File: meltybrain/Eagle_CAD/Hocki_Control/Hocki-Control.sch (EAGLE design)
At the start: 123 parts, among them J1 SM03B-SRSS-TB(LF)(SN), J2 SM03B-SRSS-TB(LF)(SN), J3 SM03B-SRSS-TB(LF)(SN), J4 SM04B-SRSS-TB(LF)(SN), J5 SM04B-SRSS-TB(LF)(SN), U1 TEENSY_4.1, U10 TLV3502AIDCNR, U11 NL27WZ32USG, U12 NL27WZ32USG, U13 HMC1052L-TR, U14 LMV358, U15 IRF7509, U16 TMUX1219DCKR, U17 LMV358, U18 LMV358, U19 AP2210K-3.3TRG1, U2 ADXL375, U20 AP2210K-5.0TRG1, U21 AP63200, U22 74AHC1G04GW,125, U23 LDL212PU50R, U3 ADXL375, U4 ADXL375, U5 ADXL375, U6 LMH6612MAX/NOPB, U7 LMH6612MAX/NOPB, U8 LMH6612MAX/NOPB, U9 LMH6612MAX/NOPB

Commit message: accs moved
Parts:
- added D3: D26V0H1U2LP20-7, Hocki_Library:D26V0H1U2LP20-7
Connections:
- net +24V: now also D3.C
- net CS3: now also U1.10/PWM/MQSR/CS; no longer U1.9/PWM/OUT1C
- net CS4: now also U1.24/PWM/SCL2/TX6/A10; no longer U1.10/PWM/MQSR/CS
- net GND: now also D3.A
- net INT1A: now also U1.41/A17; no longer U1.40/A16
- net INT1B: now also U1.40/A16; no longer U1.41/A17
- net INT3A: now also U1.7/PWM/OUT1A/RX2; no longer U1.8/PWM/IN1/TX2
- net INT3B: now also U1.8/PWM/IN1/TX2; no longer U1.7/PWM/OUT1A/RX2
- net INT4B: now also U1.26/MOSI1/A12; no longer U1.24/PWM/SCL2/TX6/A10

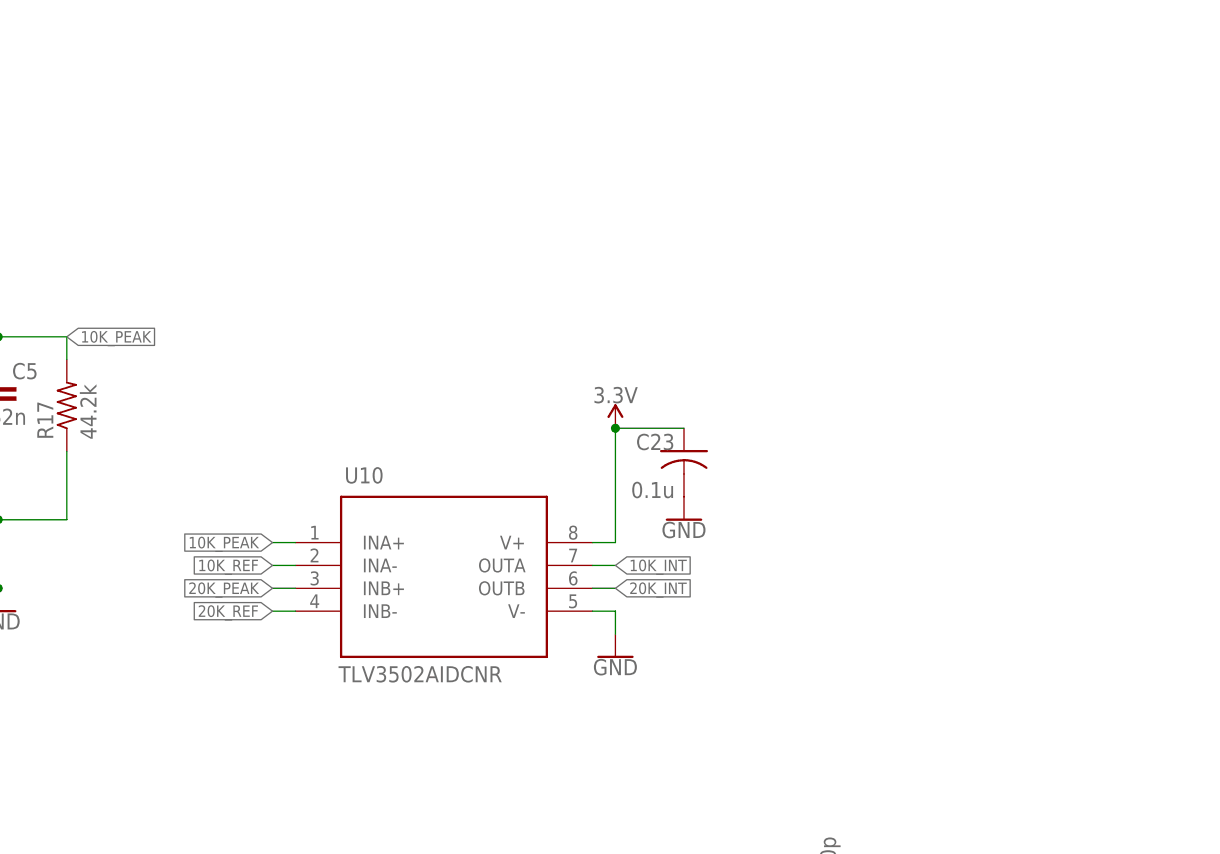
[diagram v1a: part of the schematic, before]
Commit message: added comparator hysteresis
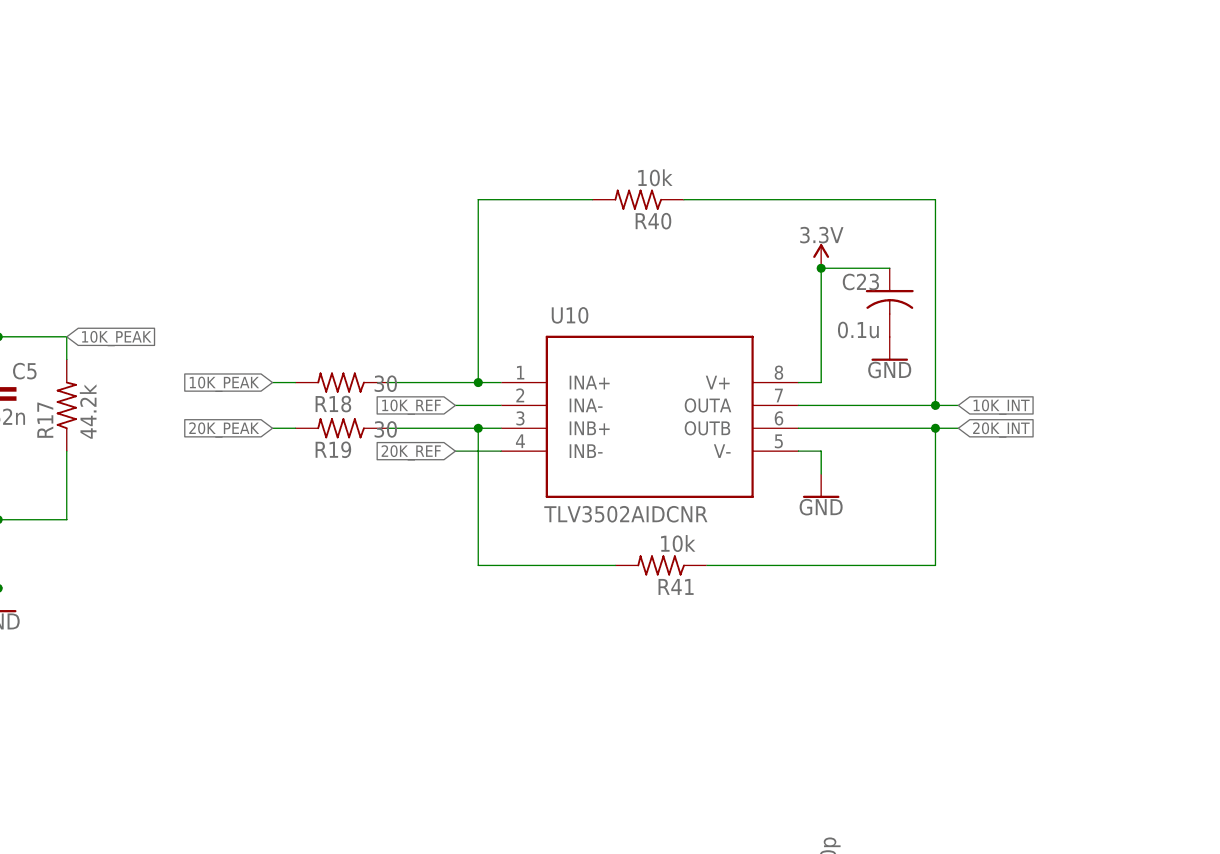
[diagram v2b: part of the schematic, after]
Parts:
- added R18, R19: 30, rcl:R-US_R0603
- added R40, R41: 10k, rcl:R-US_R0603
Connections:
- new net N$5: R18.1, R40.2, U10.INA+
- new net N$6: R19.1, R41.2, U10.INB+
- net 10K_INT: now also R40.1
- net 10K_PEAK: now also R18.2; no longer U10.INA+
- net 20K_INT: now also R41.1
- net 20K_PEAK: now also R19.2; no longer U10.INB+
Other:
- moved on the sheet: C23, U10

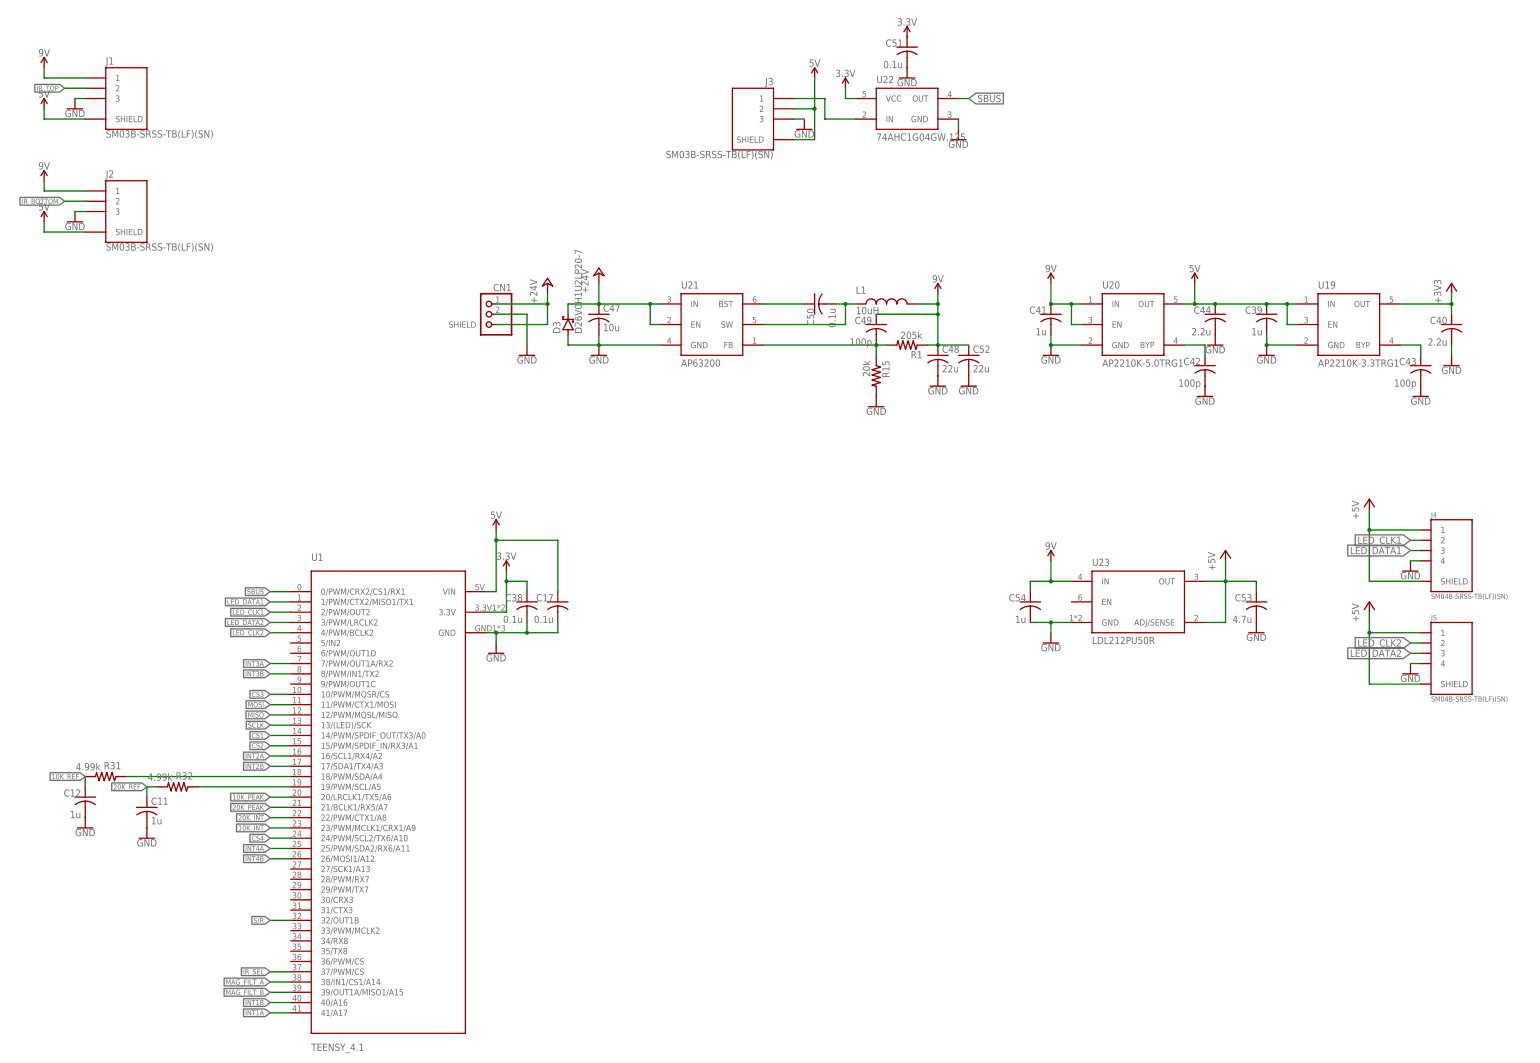
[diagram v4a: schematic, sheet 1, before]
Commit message: control schematic done
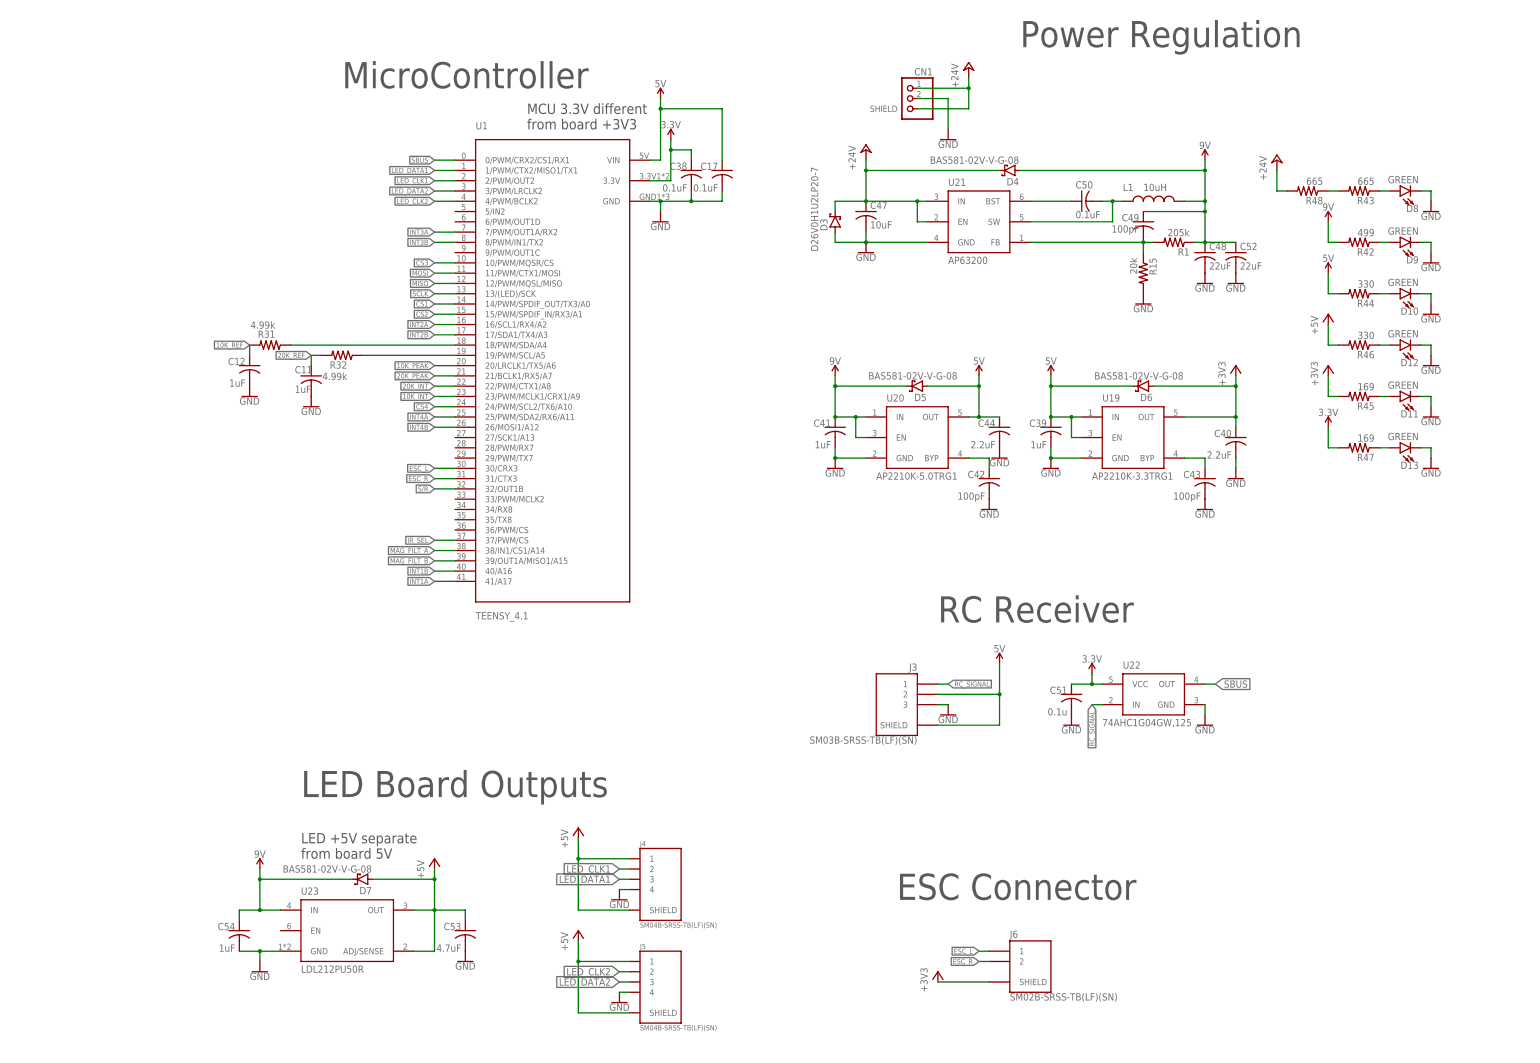
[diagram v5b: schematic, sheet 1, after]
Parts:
- added D10, D11, D12, D13, D8, D9: GREEN, SparkFun-LED:LED-GREEN0603
- added D4, D5, D6, D7: BAS581-02V-V-G-08, Hocki_Library:BAS581-02V-V-G-08
- added J6: SM02B-SRSS-TB(LF)(SN), Hocki_Library:SM02B-SRSS-TB(LF)(SN)
- added R42: 499, rcl:R-US_R0603
- added R43, R48: 665, rcl:R-US_R0603
- added R44, R46: 330, rcl:R-US_R0603
- added R45, R47: 169, rcl:R-US_R0603
- C1, C13, C15, C2, C3, C4, C45, C46: value 47n -> 47nF
- C11, C12, C39, C41, C54: value 1u -> 1uF
- C14, C16: value 0.18u -> 0.18uF
- C17, C18, C19, C20, C21, C22, C23, C24, C25, C26, C27, C28, C29, C30, C31, C32, C33, C34, C35, C36, C37, C38, C50: value 0.1u -> 0.1uF
- C40, C44: value 2.2u -> 2.2uF
- C42, C43, C49: value 100p -> 100pF
- C47: value 10u -> 10uF
- C48, C52: value 22u -> 22uF
- C5, C6: value 62n -> 62nF
- C53: value 4.7u -> 4.7uF
- C7, C9: value 1000p -> 1000pF
- C8: value .1u -> .1uF
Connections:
- net N$17 renamed RC_SIGNAL
- new net ESC_L: J6.1, U1.30/CRX3
- new net ESC_R: J6.2, U1.31/CTX3
- new net N$14: D12.A, R46.1
- new net N$15: D10.A, R44.1
- new net N$17: D11.A, R45.1
- new net N$18: D9.A, R42.1
- new net N$19: D8.A, R43.1
- new net N$20: R43.2, R48.1
- new net N$27: D13.A, R47.1
- net +24V: now also D4.C, R48.2
- net +3V3: now also D6.A, J6.SHIELD, R45.2, U14.V+, U17.V+, U18.V+; no longer U14.VCC+, U17.VCC+, U18.VCC+
- net +5V: now also D7.A, R46.2
- net 3.3V: now also R47.2
- net 5V: now also D5.A, D6.C, R44.2
- net 9V: now also D4.A, D5.C, D7.C, R42.2
- net GND: now also D10.C, D11.C, D12.C, D13.C, D8.C, D9.C, U14.V-, U17.V-, U18.INB+, U18.INB-, U18.V-; no longer U14.GND, U17.2IN+, U17.2IN-, U17.GND, U18.GND
- net MAG_FILT_A: now also U17.INA-, U17.OUTA; no longer U18.1IN-, U18.OUT
- net MAG_FILT_B: now also U17.INB-, U17.OUTB; no longer U18.2IN-, U18.2OUT
- net MAG_OUTPUTA: now also U14.OUTA; no longer U14.OUT
- net MAG_OUTPUTB: now also U14.OUTB; no longer U14.2OUT
- net N$23: now also U18.INA+; no longer U17.1IN+
- net N$24: now also U18.OUTB; no longer U17.2OUT
- net N$26: now also U17.INA+; no longer U18.1IN+
- net N$30: now also U17.INB+; no longer U18.2IN+
- net N$34: now also U14.INB-; no longer U14.2IN-
- net N$35: now also U14.INB+; no longer U14.2IN+
- net N$36: now also U14.INA-; no longer U14.1IN-
- net N$37: now also U14.INA+; no longer U14.1IN+
- net VREF/2: now also U18.INA-, U18.OUTA; no longer U17.1IN-, U17.OUT
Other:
- note added: "ESC Connector"
- note added: "LED +5V separate from board 5V"
- note added: "LED Board Outputs"
- note added: "MCU 3.3V different from board +3V3"
- note added: "MicroController"
- note added: "Power Regulation"
- note added: "RC Receiver"
- moved on the sheet: C1, C10, C11, C12, C13, C14, C15, C16, C17, C18, C19, C2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

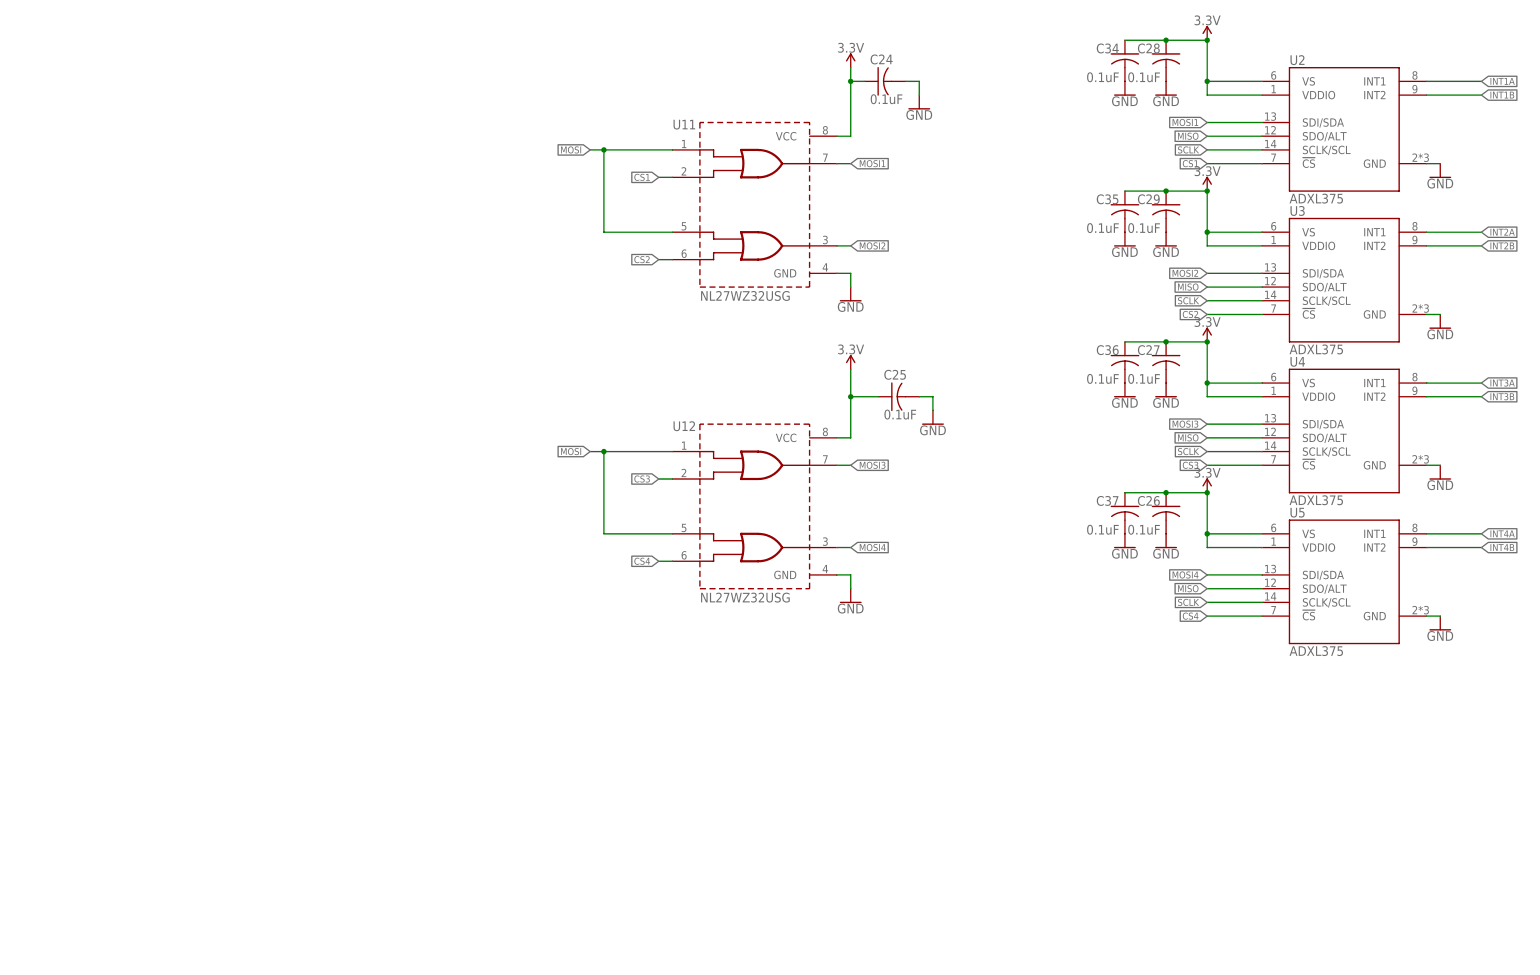
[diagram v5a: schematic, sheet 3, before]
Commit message: Edited LED board to add 3d packages.  Made cosmetic changes to Control in preparation for design review
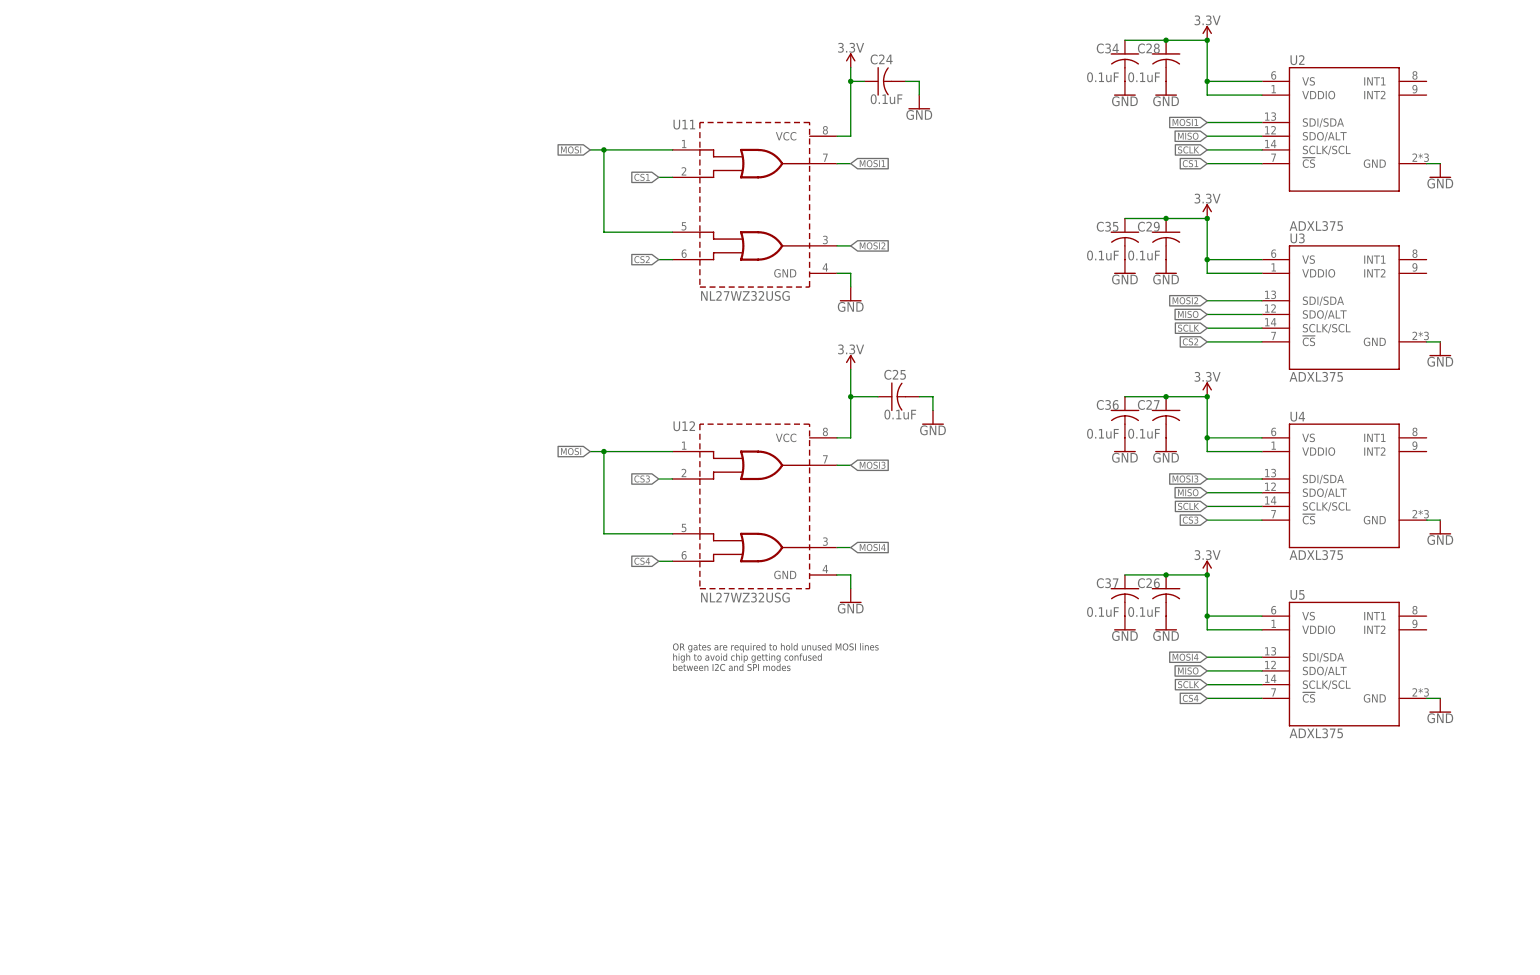
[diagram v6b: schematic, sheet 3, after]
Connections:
- removed net INT1A: U1.41/A17, U2.INT1
- removed net INT1B: U1.40/A16, U2.INT2
- removed net INT2A: U1.16/SCL1/RX4/A2, U3.INT1
- removed net INT2B: U1.17/SDA1/TX4/A3, U3.INT2
- removed net INT3A: U1.7/PWM/OUT1A/RX2, U4.INT1
- removed net INT3B: U1.8/PWM/IN1/TX2, U4.INT2
- removed net INT4A: U1.25/PWM/SDA2/RX6/A11, U5.INT1
- removed net INT4B: U1.26/MOSI1/A12, U5.INT2
- net 9V: now also U23.EN
- net ESC_L: now also U1.28/PWM/RX7; no longer U1.30/CRX3
- net ESC_R: now also U1.29/PWM/TX7; no longer U1.31/CTX3
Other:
- note added: "OR gates are required to hold unused MOSI lines high to avoid chip getting confused between I2C and SPI modes"
- note added: "SBUS is inverted UART"
- moved on the sheet: C17, C26, C27, C29, C35, C36, C37, C38, C51, J1, J2, J3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
